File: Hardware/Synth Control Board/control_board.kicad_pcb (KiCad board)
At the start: 2 copper layers, 127 x 177.8 mm, 42 parts, among them J1 Conn_01x18, J2 Conn_01x03, J3 Conn_02x18_Odd_Even, J5 Conn_01x02, SW1 SW_DPDT_x2, SW10 SW_SPST, SW11 SW_SPST, SW12 SW_SPST, SW13 SW_SPST, SW2 SW_SPST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

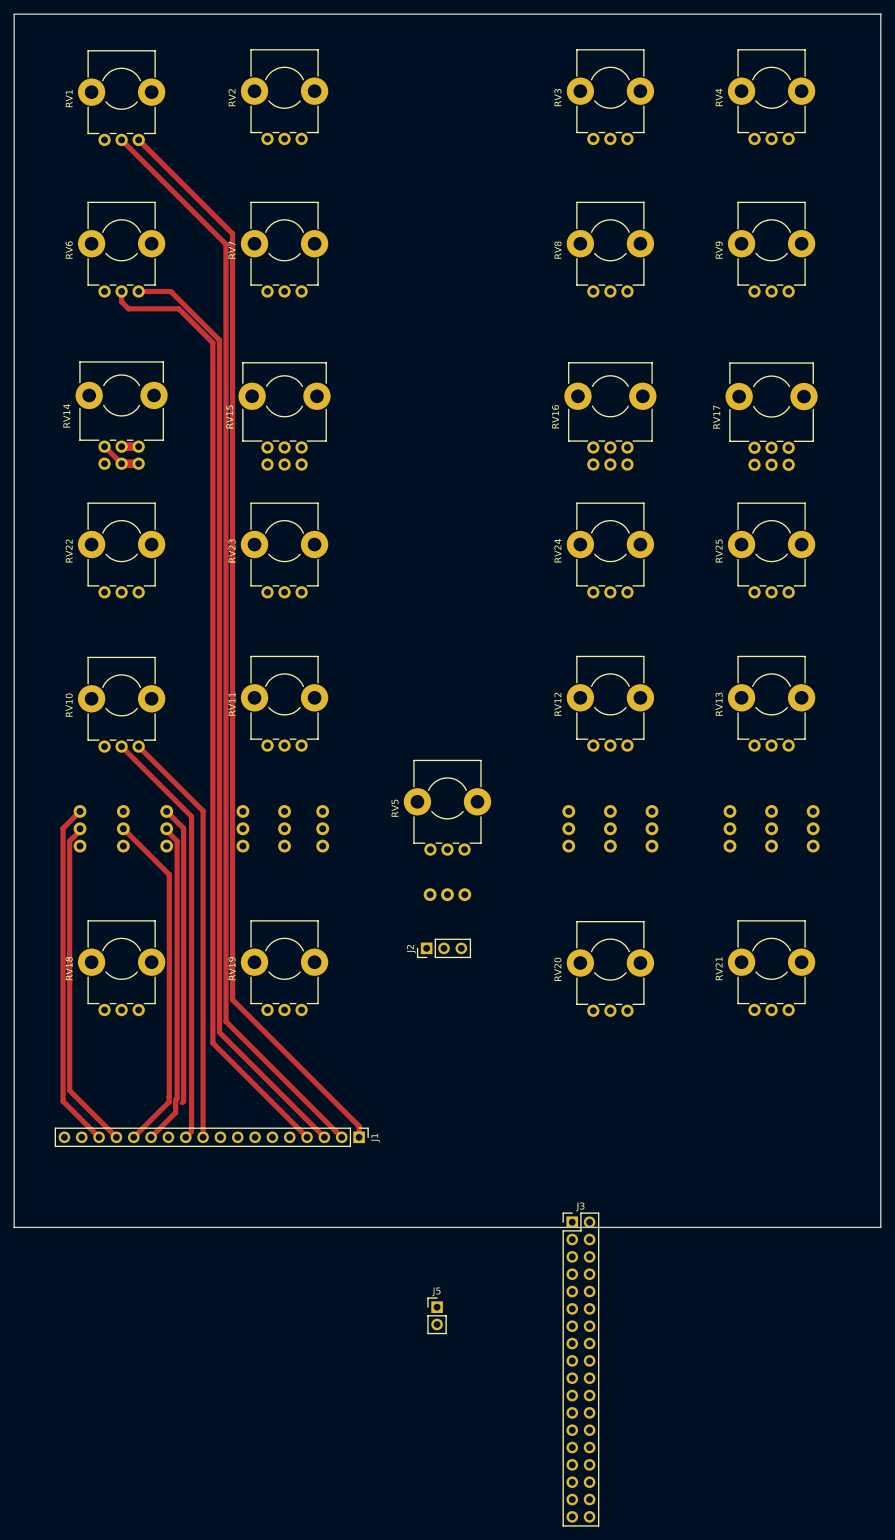
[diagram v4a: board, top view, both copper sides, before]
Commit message: route connectors on control board. Will add additional set of connectors for filter knobs to simplify routing.
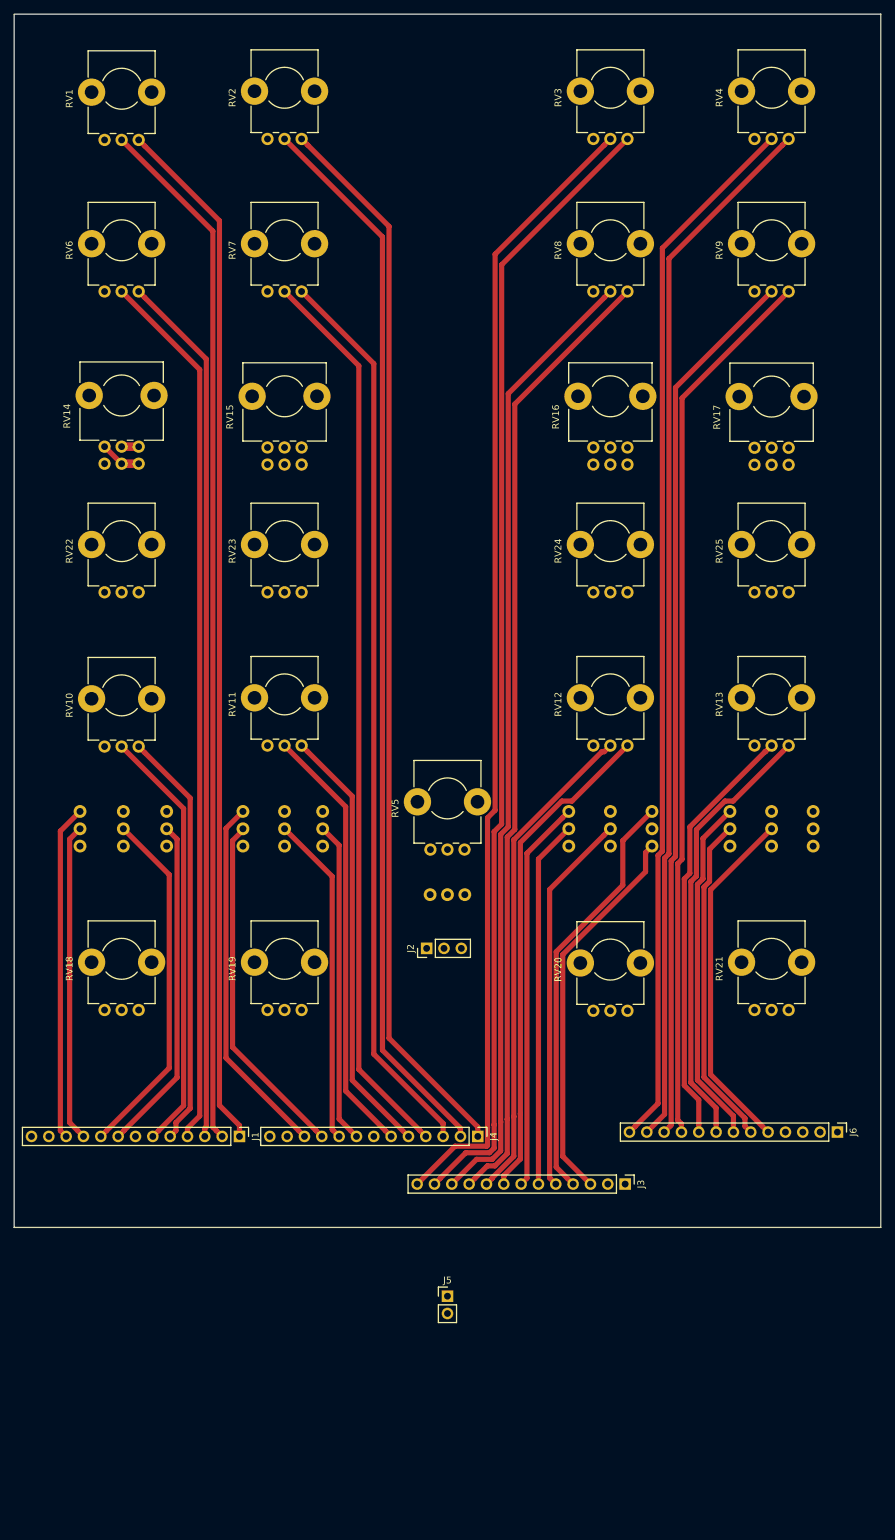
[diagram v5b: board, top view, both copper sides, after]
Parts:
- added J4: Conn_01x13, Pin_Headers:Pin_Header_Straight_1x13_Pitch2.54mm, F.Cu at (67.9, 164.5)
- added J6: Conn_01x13, Pin_Headers:Pin_Header_Straight_1x13_Pitch2.54mm, F.Cu at (120.7, 163.8)
- J1: value Conn_01x18 -> Conn_01x13; footprint Pin_Headers:Pin_Header_Straight_1x18_Pitch2.54mm -> Pin_Headers:Pin_Header_Straight_1x13_Pitch2.54mm
- J3: value Conn_02x18_Odd_Even -> Conn_01x13; footprint Pin_Headers:Pin_Header_Straight_2x18_Pitch2.54mm -> Pin_Headers:Pin_Header_Straight_1x13_Pitch2.54mm
- moved J1 17.5 mm to (33.0, 164.5)
- moved J3 9.55 mm to (89.5, 171.4), turned to 270 degrees
- moved J5 2.22 mm to (63.5, 187.9)
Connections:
- J1 pad 10: +5V -> /envelope_pwm_bypass_out_1
- J1 pad 11: /osc1_speed -> /envelope_pwm_bypass_in_1
- J1 pad 12: /osc1_hold -> GND
- J1 pad 13: /osc1_repeat -> GNDD
- J1 pad 5: /freq_in_1 -> +5V
- J1 pad 6: /freq_fb_1 -> /osc1_speed
- J1 pad 7: /freq_out_1 -> /osc1_hold
- J1 pad 8: /lfo_in_1 -> /osc1_repeat
- J1 pad 9: /lfo_out_1 -> /osc1_quant
- J3 pad 1: +5V -> GND
- J3 pad 10: /freq_out_4 -> +5V
- J3 pad 11: /freq_fb_3 -> /osc3_pwm_wiper
- J3 pad 12: /freq_fb_4 -> +5V
- J3 pad 13: /freq_in_3 -> /osc3_freq_wiper
- J3 pad 2: +5V -> GNDD
- J3 pad 3: /osc3_freq_wiper -> /osc3_hold
- J3 pad 4: /osc4_freq_wiper -> /osc3_repeat
- J3 pad 5: /osc3_pwm_wiper -> /osc3_quant
- J3 pad 6: /osc4_pwm_wiper -> /envelope_pwm_bypass_out_3
- J3 pad 7: +5V -> /envelope_pwm_bypass_in_3
- J3 pad 9: /freq_out_3 -> /osc3_speed
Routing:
- net +5V: track 358.7 -> 1424.4 mm
- net /osc3_freq_wiper: track 0.00 -> 167.6 mm
- net /osc2_freq_wiper: track 0.00 -> 156.9 mm
- net /osc4_freq_wiper: track 0.00 -> 154.2 mm
- net /osc3_pwm_wiper: track 0.00 -> 141.8 mm
- net /osc2_pwm_wiper: track 0.00 -> 132.4 mm
- net /osc4_pwm_wiper: track 0.00 -> 129.7 mm
- net /osc3_speed: track 0.00 -> 72.0 mm
- net /osc2_speed: track 0.00 -> 63.7 mm
- net /osc4_speed: track 0.00 -> 62.9 mm
- net /osc3_repeat: track 0.00 -> 61.5 mm
- net /envelope_pwm_bypass_in_3: track 0.00 -> 57.5 mm
- net /osc3_hold: track 0.00 -> 56.6 mm
- net /osc3_quant: track 0.00 -> 56.1 mm
- net /envelope_pwm_bypass_out_3: track 0.00 -> 53.9 mm
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
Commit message: fix SPDT hold/repeat switches on control board
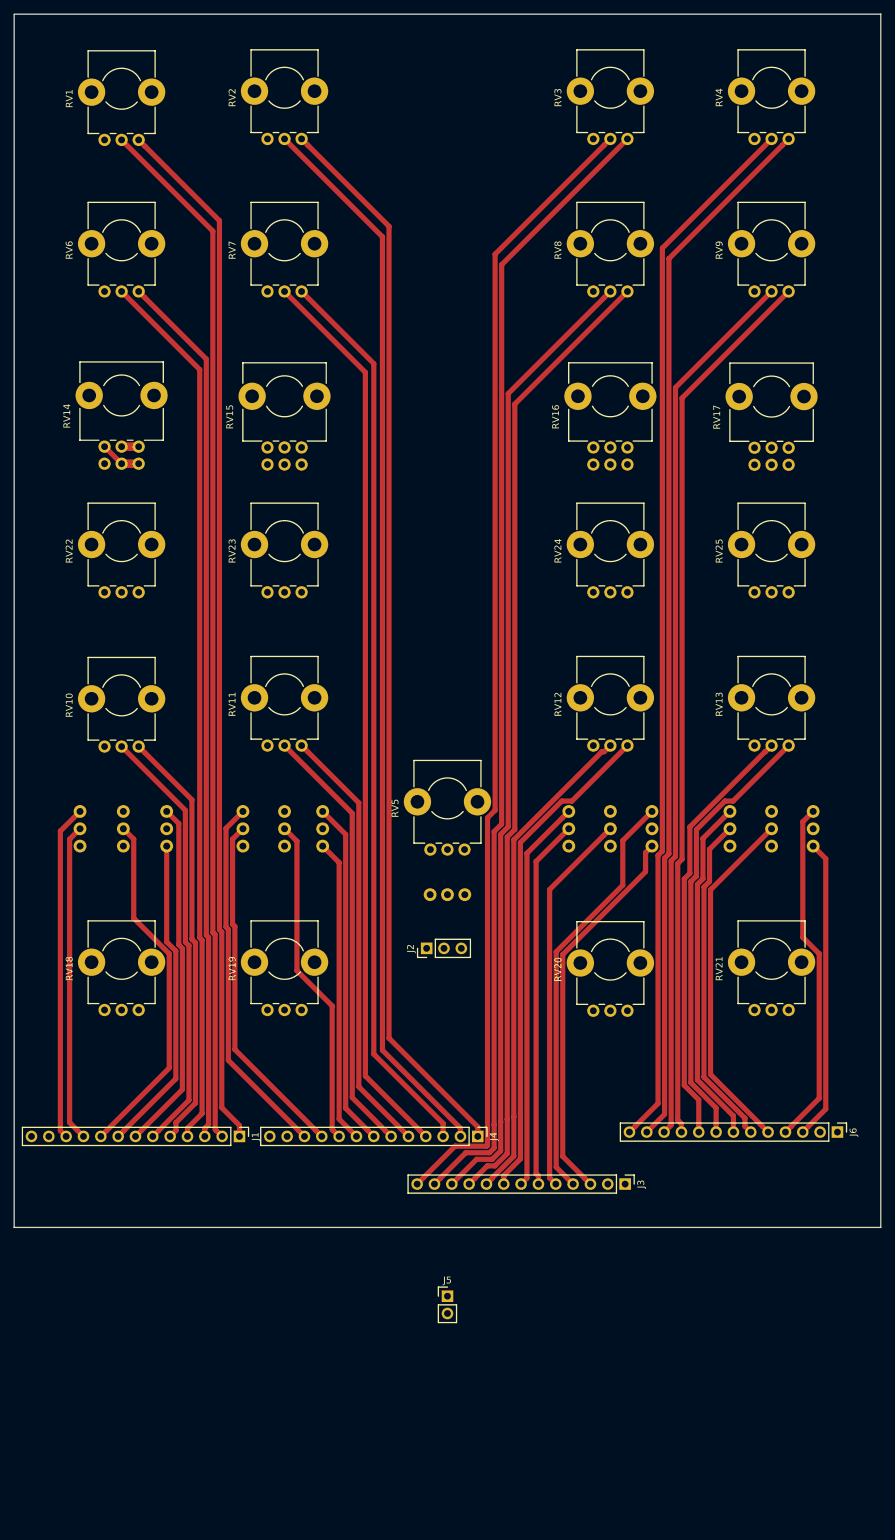
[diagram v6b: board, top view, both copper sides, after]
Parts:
- SW6, SW7: value SW_DPDT_x2 -> SW_SPDT
- SW8, SW9: value SW_SPST -> SW_SPDT
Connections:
- J3 pad 3: /osc3_hold -> /osc3_repeat
- J3 pad 4: /osc3_repeat -> /osc3_hold
- J6 pad 3: /osc4_hold -> /osc4_repeat
- J6 pad 4: /osc4_repeat -> /osc4_hold
- SW6 pad 1: /osc1_repeat -> /osc4_hold
- SW6 pad 3: /osc1_hold -> /osc4_repeat
- SW7 pad 1: /osc3_repeat -> /osc3_hold
- SW7 pad 3: /osc3_hold -> /osc3_repeat
- SW8 pad 1: GNDD -> /osc2_hold
- SW8 pad 2: /osc2_repeat -> GNDD
- SW8 pad 3: (no net) -> /osc2_repeat
- SW9 pad 1: GNDD -> /osc1_hold
- SW9 pad 2: /osc1_repeat -> GNDD
- SW9 pad 3: (no net) -> /osc1_repeat
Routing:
- net /osc1_hold: track 0.00 -> 51.6 mm
- net /osc2_hold: track 0.00 -> 50.7 mm
- net /osc4_hold: track 0.00 -> 50.7 mm
- net /osc4_repeat: track 0.00 -> 44.1 mm
- net /osc3_repeat: track 61.5 -> 56.6 mm
- net /osc3_hold: track 56.6 -> 61.5 mm
- net /osc1_repeat: track 49.3 -> 46.6 mm
- net /osc2_repeat: track 47.1 -> 44.6 mm
- net +5V: track 1424.4 -> 1425.4 mm
- net /osc1_speed: track 62.8 -> 63.4 mm

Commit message: add copper pour GND layer to control board
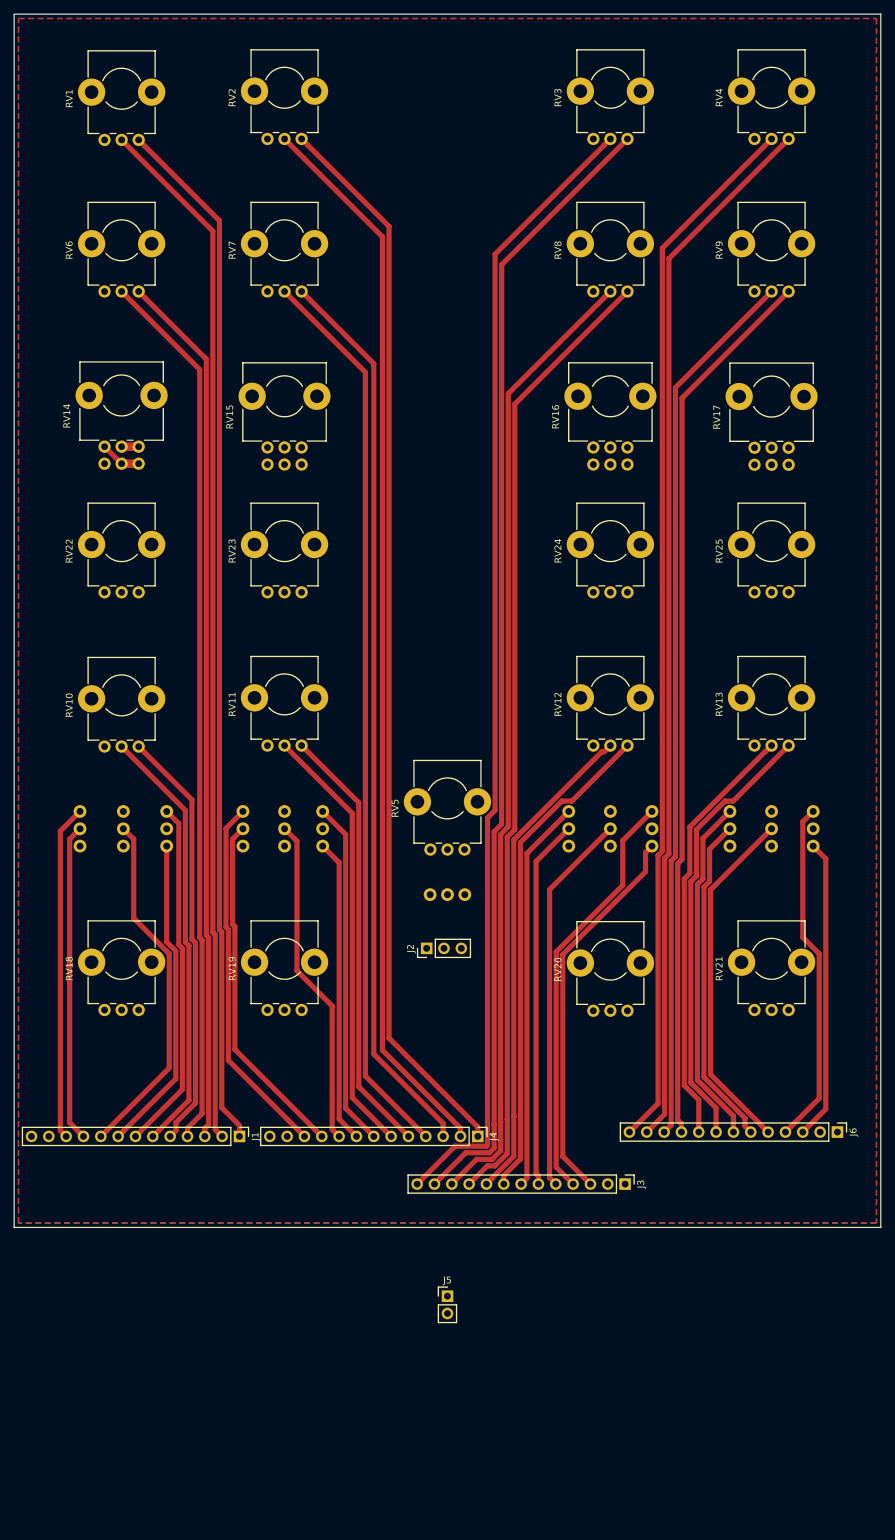
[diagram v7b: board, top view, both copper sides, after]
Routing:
- added copper zone on B.Cu, net GND
- added copper zone on F.Cu, net GND
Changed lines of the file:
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@@
   (segment (start 51.855001 163.615001) (end 52.705 164.465) (width 0.762) (layer F.Cu) (net 68))
   (segment (start 48.587011 160.347011) (end 51.855001 163.615001) (width 0.762) (layer F.Cu) (net 68))
+  (zone (net 12) (net_name GND) (layer F.Cu) (hatch edge 0.508)
+    (connect_pads (clearance 0.508))
+    (min_thickness 0.254)
+    (fill yes (arc_segments 16) (thermal_gap 0.508) (thermal_bridge_width 0.508))
+    (polygon
+      (pts
+        (xy 0.635 0.635) (xy 126.365 0.635) (xy 126.365 177.165) (xy 0.635 177.165)
+      )
+    )
+  )
+  (zone (net 12) (net_name GND) (layer B.Cu) (hatch edge 0.508)
+    (connect_pads (clearance 0.508))
+    (min_thickness 0.254)
+    (fill yes (arc_segments 16) (thermal_gap 0.508) (thermal_bridge_width 0.508))
+    (polygon
+      (pts
+        (xy 0.635 0.635) (xy 126.365 0.635) (xy 126.365 177.165) (xy 0.635 177.165)
+      )
+    )
+  )
 )

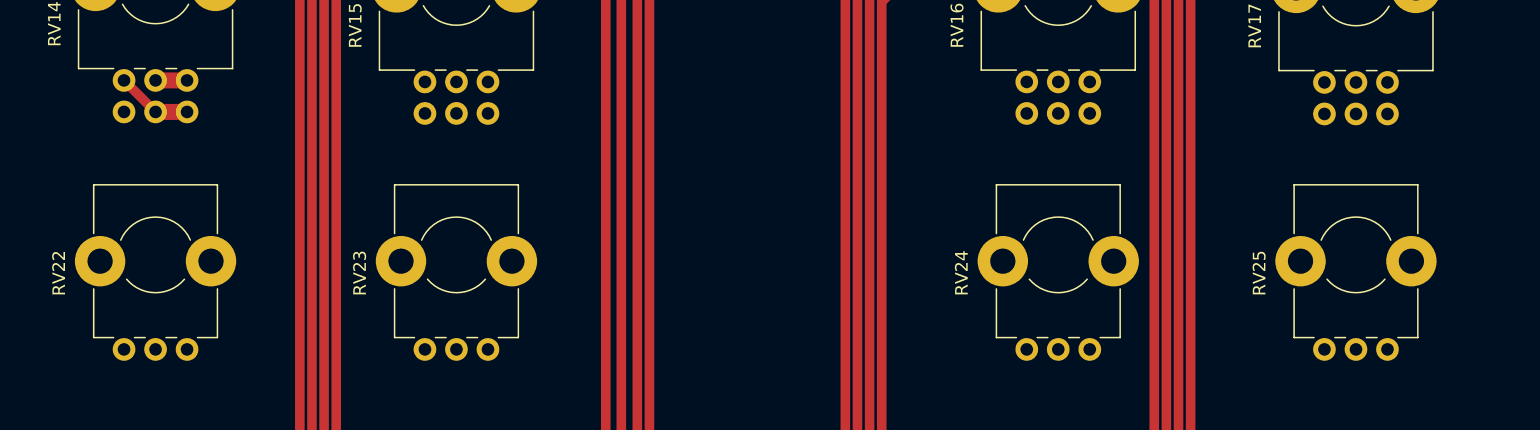
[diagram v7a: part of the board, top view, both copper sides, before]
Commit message: add frequency and LFO connectors to control board
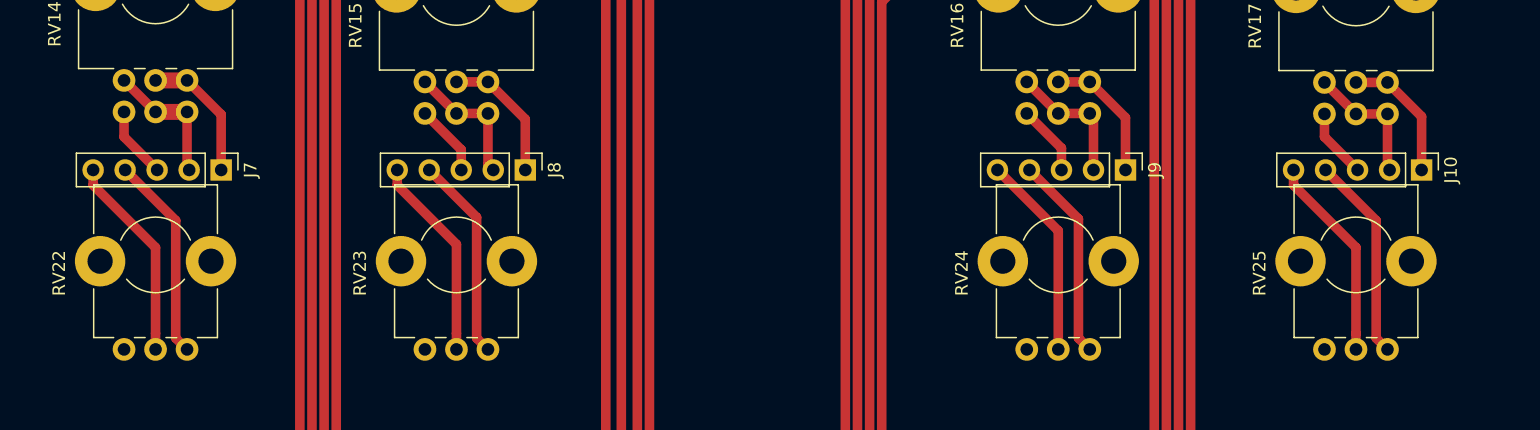
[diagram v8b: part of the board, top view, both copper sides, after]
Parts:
- added J10: Conn_01x05, Pin_Headers:Pin_Header_Straight_1x05_Pitch2.54mm, F.Cu at (116.2, 70.5)
- added J7: Conn_01x05, Pin_Headers:Pin_Header_Straight_1x05_Pitch2.54mm, F.Cu at (21.0, 70.5)
- added J8: Conn_01x05, Pin_Headers:Pin_Header_Straight_1x05_Pitch2.54mm, F.Cu at (45.1, 70.5)
- added J9: Conn_01x05, Pin_Headers:Pin_Header_Straight_1x05_Pitch2.54mm, F.Cu at (92.7, 70.5)
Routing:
- net /lfo_out_4: track 0.00 -> 16.3 mm
- net /lfo_out_1: track 0.00 -> 16.3 mm
- net /lfo_in_4: track 0.00 -> 16.3 mm
- net /lfo_in_1: track 0.00 -> 16.3 mm
- net /lfo_out_3: track 0.00 -> 16.2 mm
- net /lfo_in_3: track 0.00 -> 16.2 mm
- net /lfo_out_2: track 0.00 -> 16.2 mm
- net /lfo_in_2: track 0.00 -> 16.2 mm
- net /freq_in_2: track 0.00 -> 10.7 mm
- net /freq_fb_2: track 0.00 -> 10.7 mm
- net /freq_in_3: track 0.00 -> 10.7 mm
- net /freq_fb_3: track 0.00 -> 10.6 mm
- net /freq_in_4: track 0.00 -> 10.6 mm
- net /freq_fb_4: track 0.00 -> 10.5 mm
- net /freq_in_1: track 2.50 -> 10.7 mm
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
